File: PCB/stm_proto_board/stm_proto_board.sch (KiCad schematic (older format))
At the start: 23 parts, among them J1 Conn_01x08_Female, J2 Conn_01x04, J3 DB9_Female, J4 Conn_01x02, SW1 SW_Push, SW2 SW_Push, SW3 SW_Push, SW4 SW_Push, U1 STM32F103C8T6_shield, U2 MCP2551-I-P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

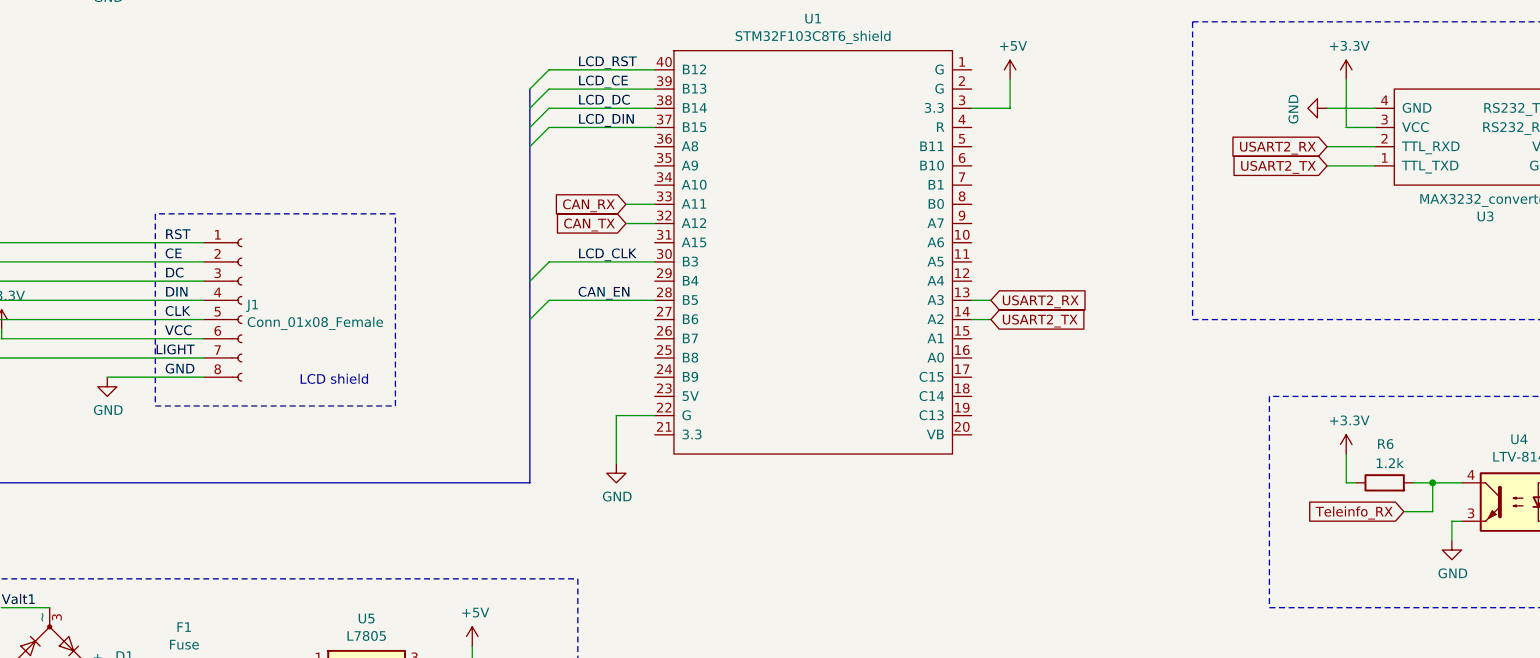
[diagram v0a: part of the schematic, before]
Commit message: Add PWM + template code for other modules
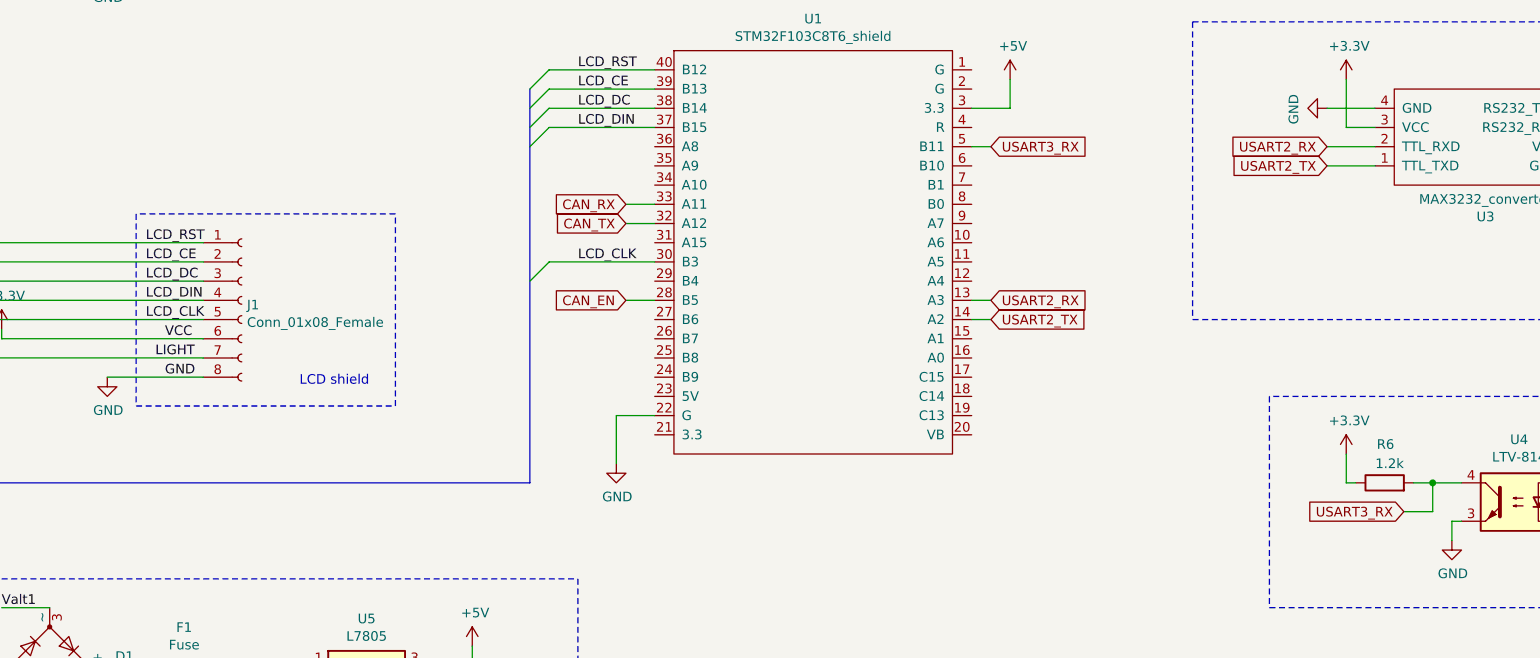
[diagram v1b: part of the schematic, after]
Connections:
- net CE is gone; now on net LCD_CE: J1.2 (Pin_2)
- net CLK is gone; now on net LCD_CLK: J1.5 (Pin_5)
- net DC is gone; now on net LCD_DC: J1.3 (Pin_3)
- net DIN is gone; now on net LCD_DIN: J1.4 (Pin_4)
- net RST is gone; now on net LCD_RST: J1.1 (Pin_1)
- net Teleinfo_RX is gone; now on net USART3_RX: R6.2, U4.4
- net USART3_RX: now reaches U1.5 (B11)
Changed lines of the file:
@@
 	1    0    0    -1
 $EndComp
-Text Label 2150 4250 0    50   ~ 0
-RST
-Text Label 2150 4350 0    50   ~ 0
-CE
-Text Label 2150 4450 0    50   ~ 0
-DC
-Text Label 2150 4550 0    50   ~ 0
-DIN
-Text Label 2150 4650 0    50   ~ 0
-CLK
+Text Label 2050 4250 0    50   ~ 0
+LCD_RST
+Text Label 2050 4350 0    50   ~ 0
+LCD_CE
+Text Label 2050 4450 0    50   ~ 0
+LCD_DC
+Text Label 2050 4550 0    50   ~ 0
+LCD_DIN
+Text Label 2050 4650 0    50   ~ 0
+LCD_CLK
 Text Label 2150 4750 0    50   ~ 0
 VCC
@@
 	8300 5500 8350 5500
 Text GLabel 8600 5650 0    50   Input ~ 0
-Teleinfo_RX
+USART3_RX
 Wire Wire Line
 	8650 5500 8750 5500
@@
 	4300 7500 800  7500
 Wire Notes Line
-	2100 4100 2100 5100
-Wire Notes Line
-	2100 5100 3350 5100
+	2000 4100 2000 5100
 Wire Notes Line
 	3350 5100 3350 4100
-Wire Notes Line
-	3350 4100 2100 4100
 Text Notes 2850 5000 0    50   ~ 0
 LCD shield
@@
 Wire Wire Line
 	4150 4350 4700 4350
-Text Label 4300 4550 0    50   ~ 0
-CAN_EN
-Wire Wire Line
-	4150 4550 4700 4550
 Entry Wire Line
 	4050 3450 4150 3350
@@
 Entry Wire Line
 	4050 3650 4150 3550
-Entry Wire Line
-	4050 4650 4150 4550
 Entry Wire Line
 	4050 4450 4150 4350
@@
 Wire Wire Line
 	6350 3550 6550 3550
+Text GLabel 6450 3750 2    50   Input ~ 0
+USART3_RX
+Wire Wire Line
+	6350 3750 6450 3750
+Text GLabel 4550 4550 0    50   Input ~ 0
+CAN_EN
+Wire Wire Line
+	4700 4550 4550 4550
+Wire Notes Line
+	3350 4100 2000 4100
+Wire Notes Line
+	2000 5100 3350 5100
+Wire Bus Line
+	4050 3450 4050 5500
 Wire Bus Line
 	900  4350 900  5500
-Wire Bus Line
-	4050 3450 4050 5500
 $EndSCHEMATC

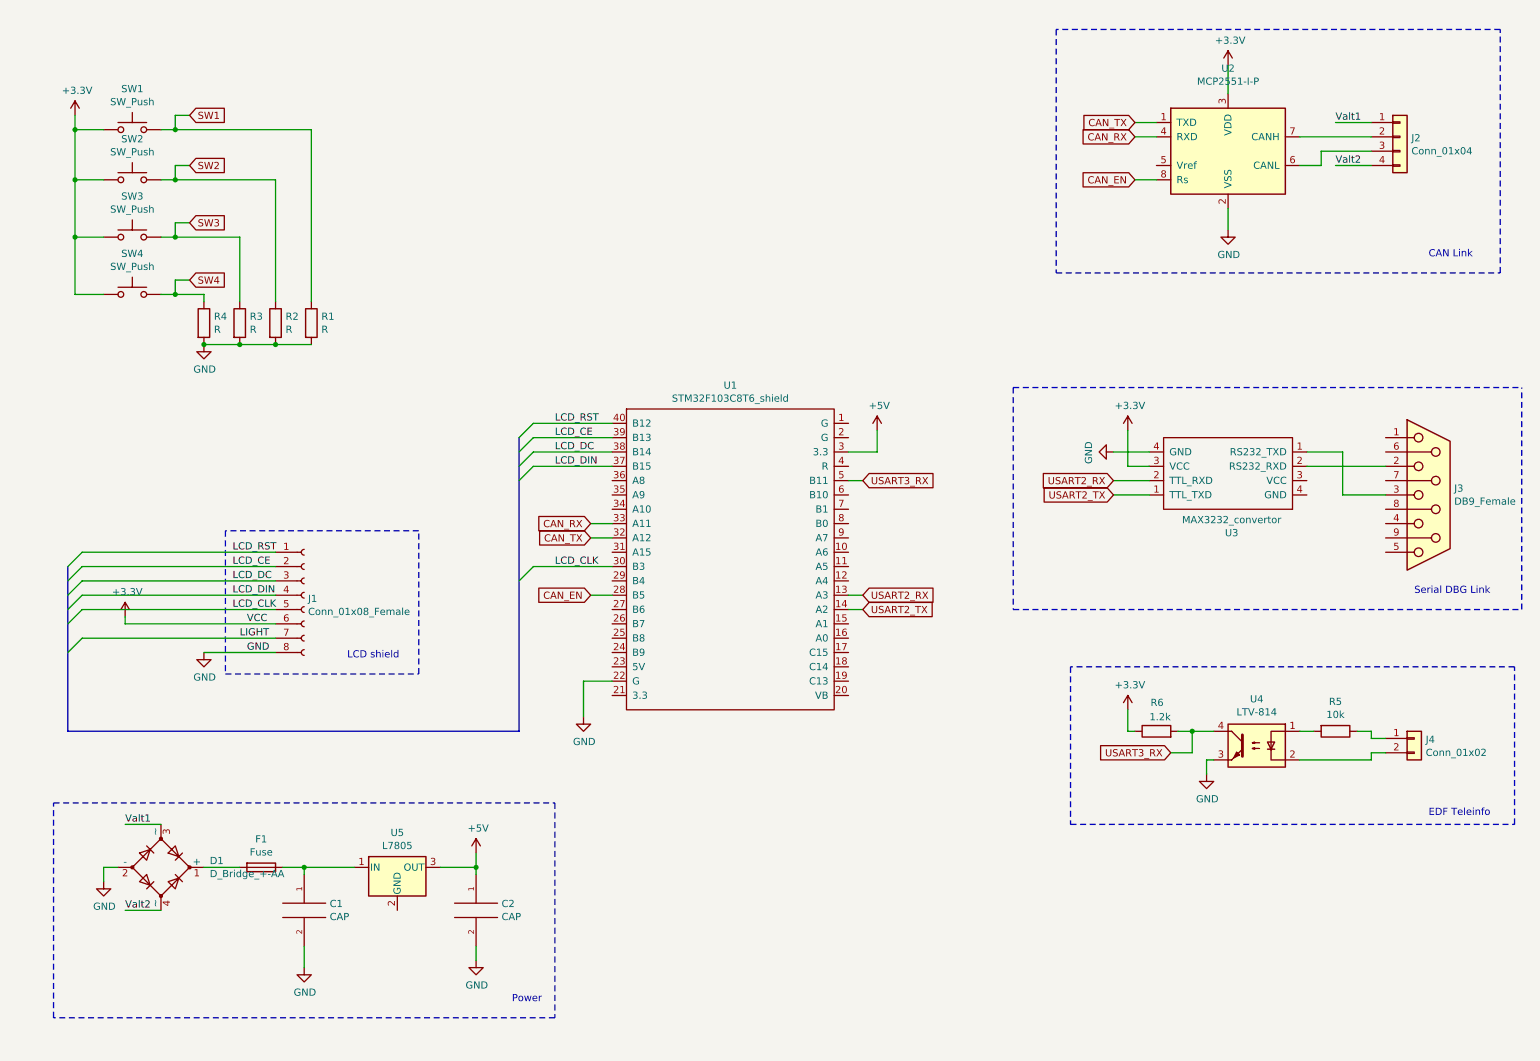
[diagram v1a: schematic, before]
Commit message: LedStrip management
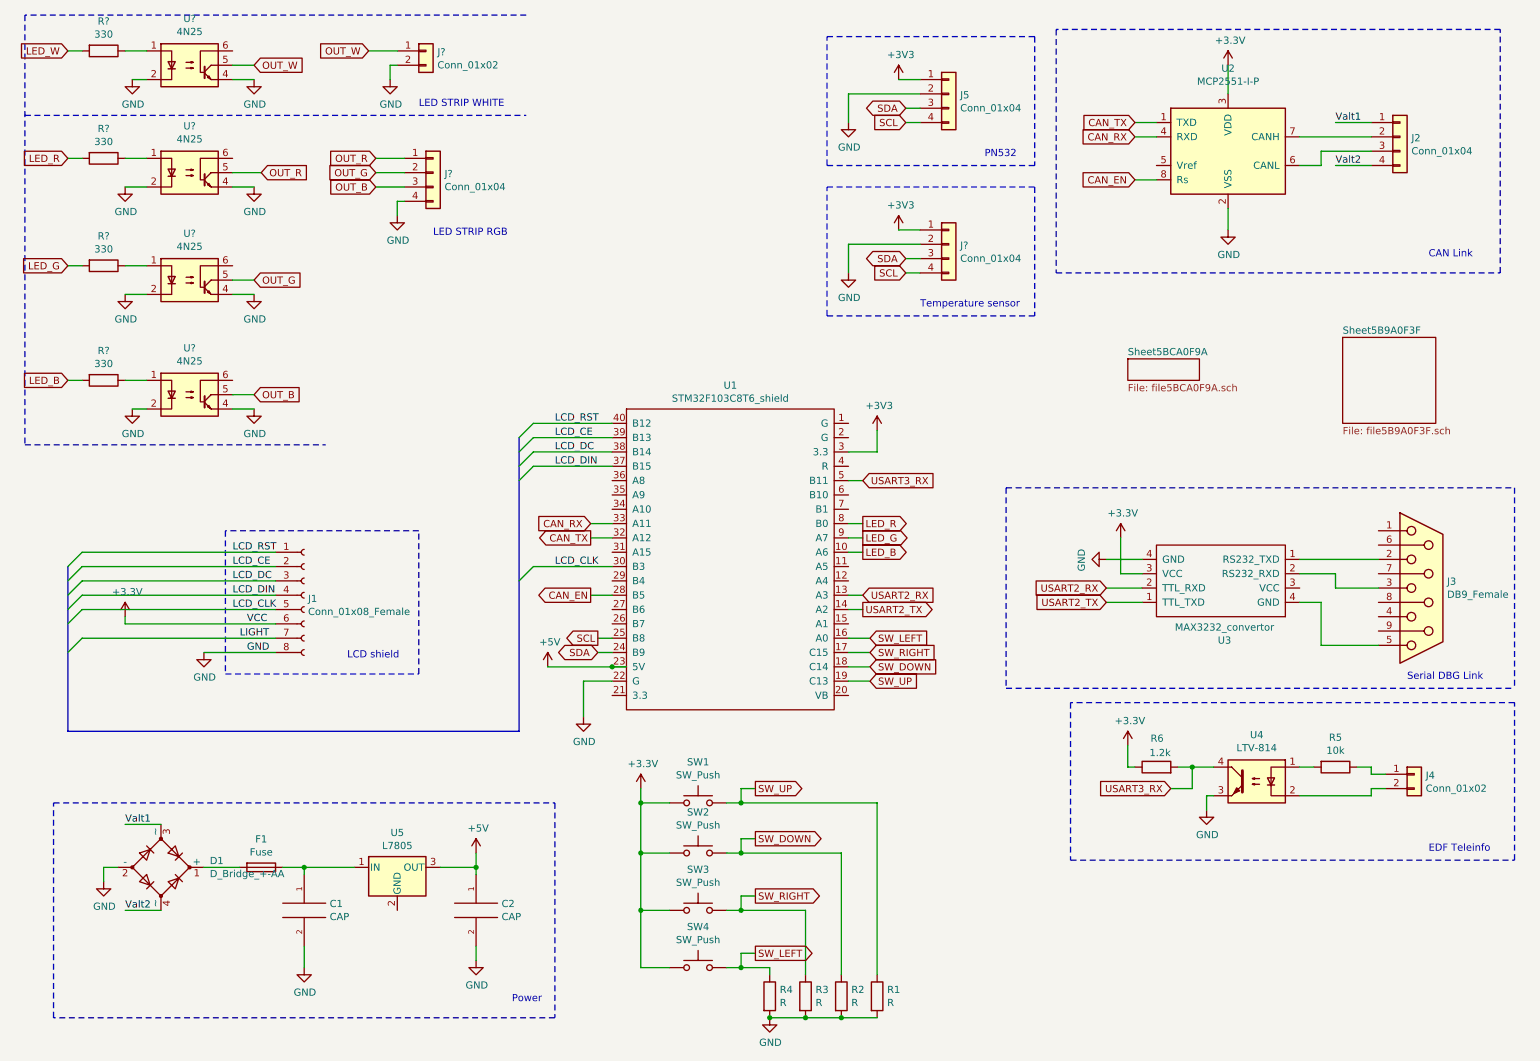
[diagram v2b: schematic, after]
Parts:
- added J5, J? (x2): Conn_01x04, Connector_Wire:SolderWirePad_1x04_P3.81mm_Drill1mm, symbol Connector_Generic:Conn_01x04
- added J?: Conn_01x02, symbol Connector_Generic:Conn_01x02
- added R? (x4): 330, Resistor_THT:R_Axial_DIN0204_L3.6mm_D1.6mm_P7.62mm_Horizontal, symbol Device:R
- added U? (x4): 4N25, Package_DIP:DIP-6_W7.62mm, symbol Isolator:4N25
- J2: footprint (none) -> Connector_Wire:SolderWirePad_1x04_P3.81mm_Drill1mm
- R1, R2, R3, R4, R5, R6: footprint (none) -> Resistor_THT:R_Axial_DIN0204_L3.6mm_D1.6mm_P7.62mm_Horizontal
- SW1, SW2, SW3, SW4: footprint (none) -> Button_Switch_THT:SW_PUSH_6mm
- U5: footprint (none) -> Package_TO_SOT_THT:TO-220-3_Vertical
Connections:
- net SW1 is gone; now on net SW_UP: R1.1, SW1.2
- net SW2 is gone; now on net SW_DOWN: R2.1, SW2.2
- net SW3 is gone; now on net SW_RIGHT: R3.1, SW3.2
- net SW4 is gone; now on net SW_LEFT: R4.1, SW4.2
- net +3V3: now also U1.3 (3.3), J5.1 (Pin_1), J?.1 (Pin_1)
- net +5V: now also U1.23 (5V); no longer U1.3 (3.3)
- net GND: now also J5.2 (Pin_2), J?.2 (Pin_2), J?.2 (Pin_2), J?.4 (Pin_4), U?.2, U?.2, U?.2, U?.2, U?.4, U?.4, U?.4, U?.4
- net at J3.2: now also U3.1 (TTL_TXD); no longer U3.2 (TTL_RXD)
- net at J3.3: now also U3.2 (TTL_RXD); no longer U3.1 (TTL_TXD)
- net at J3.5: now also U3.4 (GND)
- net LED_B: now reaches U1.10 (A6)
- net LED_B: now also R?.2
- net SW_LEFT: now reaches U1.16 (A0)
- net SW_RIGHT: now reaches U1.17 (C15)
- net SW_DOWN: now reaches U1.18 (C14)
- net SW_UP: now reaches U1.19 (C13)
- net SDA: now reaches U1.24 (B9)
- net SDA: now also J5.3 (Pin_3), J?.3 (Pin_3)
- net SCL: now reaches U1.25 (B8)
- net SCL: now also J5.4 (Pin_4), J?.4 (Pin_4)
- net LED_R: now reaches U1.8 (B0)
- net LED_R: now also R?.2
- net LED_G: now reaches U1.9 (A7)
- net LED_G: now also R?.2
- new net: R?.1, U?.1 (x4)
- new net LED_W: R?.2
- new net OUT_B: J?.3 (Pin_3), U?.5
- new net OUT_G: J?.2 (Pin_2), U?.5
- new net OUT_R: J?.1 (Pin_1), U?.5
- new net OUT_W: J?.1 (Pin_1), U?.5
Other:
- note added: "LED STRIP RGB"
- note added: "LED STRIP WHITE"
- note added: "PN532"
- note added: "Temperature sensor"
- moved on the sheet: J3, J4, R1, R2, R3, R4, R5, R6, SW1, SW2, SW3, SW4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

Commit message: current verson of schematic
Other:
- moved on the sheet: J?
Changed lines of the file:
@@
 EESchema Schematic File Version 4
-LIBS:stm_proto_board-cache
-EELAYER 26 0
+EELAYER 30 0
 EELAYER END
 $Descr A4 11693 8268
@@
 Wire Wire Line
 	1300 3050 1450 3050
-Text GLabel 2250 1600 2    50   Input ~ 0
-OUT_R
-Text GLabel 2200 2350 2    50   Input ~ 0
-OUT_G
-Text GLabel 2200 3150 2    50   Input ~ 0
-OUT_B
 $Comp
 L power:GND #PWR0129
 U 1 1 5BB06CFC
-P 3200 1900
-F 0 "#PWR0129" H 3200 1650 50  0001 C CNN
-F 1 "GND" H 3205 1727 50  0000 C CNN
-F 2 "" H 3200 1900 50  0001 C CNN
-F 3 "" H 3200 1900 50  0001 C CNN
-	1    3200 1900
-	1    0    0    -1
-$EndComp
-Text Notes 3450 2050 0    50   ~ 0
+P 3200 2000
+F 0 "#PWR0129" H 3200 1750 50  0001 C CNN
+F 1 "GND" H 3205 1827 50  0000 C CNN
+F 2 "" H 3200 2000 50  0001 C CNN
+F 3 "" H 3200 2000 50  0001 C CNN
+	1    3200 2000
+	1    0    0    -1
+$EndComp
+Text Notes 3450 2150 0    50   ~ 0
 LED STRIP RGB
 $Comp
 L Connector_Generic:Conn_01x04 J?
 U 1 1 5BB06CEF
-P 3450 1600
-F 0 "J?" H 3530 1592 50  0000 L CNN
-F 1 "Conn_01x04" H 3530 1501 50  0000 L CNN
-F 2 "Connector_Wire:SolderWirePad_1x04_P3.81mm_Drill1mm" H 3450 1600 50  0001 C CNN
-F 3 "~" H 3450 1600 50  0001 C CNN
-	1    3450 1600
-	1    0    0    -1
-$EndComp
-Wire Wire Line
-	3250 1800 3200 1800
-Wire Wire Line
-	3200 1800 3200 1900
-Text GLabel 3050 1700 0    50   Input ~ 0
-OUT_B
-Text GLabel 3050 1600 0    50   Input ~ 0
-OUT_G
-Text GLabel 3050 1500 0    50   Input ~ 0
-OUT_R
-Wire Wire Line
-	3050 1500 3250 1500
-Wire Wire Line
-	3250 1600 3050 1600
-Wire Wire Line
-	3050 1700 3250 1700
-$Comp
-L power:GND #PWR0130
-U 1 1 5BBD2E1F
-P 3150 950
-F 0 "#PWR0130" H 3150 700 50  0001 C CNN
-F 1 "GND" H 3155 777 50  0000 C CNN
-F 2 "" H 3150 950 50  0001 C CNN
-F 3 "" H 3150 950 50  0001 C CNN
-	1    3150 950
-	1    0    0    -1
-$EndComp
-Wire Wire Line
-	3200 850  3150 850
-Wire Wire Line
-	3150 850  3150 950
-Text GLabel 3000 750  0    50   Input ~ 0
-OUT_W
-Wire Wire Line
-	3000 750  3200 750
+P 3450 1700
+F 0 "J?" H 3530 1692 50  0000 L CNN
+F 1 "Conn_01x04" H 3530 1601 50  0000 L CNN
+F 2 "Connector_Wire:SolderWirePad_1x04_P3.81mm_Drill1mm" H 3450 1700 50  0001 C CNN
+F 3 "~" H 3450 1700 50  0001 C CNN
+	1    3450 1700
+	1    0    0    -1
+$EndComp
+Wire Wire Line
+	3250 1900 3200 1900
+Wire Wire Line
+	3200 1900 3200 2000
 Wire Wire Line
 	9650 4900 9650 4600
@@
 Wire Notes Line
 	6200 1700 7650 1700
-Wire Wire Line
-	2050 1600 2250 1600
-Wire Wire Line
-	2050 2350 2200 2350
-Wire Wire Line
-	2050 3150 2200 3150
 $Comp
 L power:GND #PWR?
@@
 Wire Wire Line
 	1300 750  1450 750
-Text GLabel 2200 850  2    50   Input ~ 0
-OUT_W
-Wire Wire Line
-	2050 850  2200 850
-$Comp
-L Connector_Generic:Conn_01x02 J?
-U 1 1 5BCFD8FC
-P 3400 750
-F 0 "J?" H 3480 742 50  0000 L CNN
-F 1 "Conn_01x02" H 3480 651 50  0000 L CNN
-F 2 "" H 3400 750 50  0001 C CNN
-F 3 "~" H 3400 750 50  0001 C CNN
-	1    3400 750
-	1    0    0    -1
-$EndComp
 Text Notes 3350 1150 0    50   ~ 0
 LED STRIP WHITE
-Wire Notes Line
-	600  3500 2700 3500
 Wire Notes Line
 	600  1200 4100 1200
@@
 F1 "file5BCA0F9A.sch" 50
 $EndSheet
+Wire Wire Line
+	2850 1800 3250 1800
+Wire Wire Line
+	2050 3150 2850 3150
+Wire Wire Line
+	2050 2350 2750 2350
+Wire Wire Line
+	2750 1700 2750 2350
+Wire Wire Line
+	2850 1800 2850 3150
+Wire Wire Line
+	2050 1600 3250 1600
+Wire Wire Line
+	2750 1700 3250 1700
+$Comp
+L Connector_Generic:Conn_01x02 J?
+U 1 1 5BCFD8FC
+P 3450 850
+F 0 "J?" H 3530 842 50  0000 L CNN
+F 1 "Conn_01x02" H 3530 751 50  0000 L CNN
+F 2 "" H 3450 850 50  0001 C CNN
+F 3 "~" H 3450 850 50  0001 C CNN
+	1    3450 850
+	1    0    0    -1
+$EndComp
+$Comp
+L power:GND #PWR0130
+U 1 1 5BBD2E1F
+P 3100 950
+F 0 "#PWR0130" H 3100 700 50  0001 C CNN
+F 1 "GND" H 3105 777 50  0000 C CNN
+F 2 "" H 3100 950 50  0001 C CNN
+F 3 "" H 3100 950 50  0001 C CNN
+	1    3100 950
+	1    0    0    -1
+$EndComp
+Wire Wire Line
+	2050 850  3250 850
+Wire Wire Line
+	3100 950  3250 950
+Text Label 2950 1600 0    50   ~ 0
+OUT_R
+Text Label 2950 1700 0    50   ~ 0
+OUT_G
+Text Label 2950 1800 0    50   ~ 0
+OUT_B
+Text Label 2900 850  0    50   ~ 0
+OUT_W
 Wire Bus Line
 	4050 3450 4050 5500
